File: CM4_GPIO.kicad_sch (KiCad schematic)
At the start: 17 parts, among them J1 Conn_01x02, J14 Conn_02x03_Odd_Even, J8 THD-20-R, U3 MagJack-A70-112-331N126, U5 74LVC1G07SE-7

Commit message: added a lot more parts
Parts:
- C1: value 100n -> 0.1uF; DK (none) -> 478-KGM05AR71C104KHCT-ND; PARTNO (none) -> KGM05AR71C104KH; Part Description 0.1uF 10% 16V Ceramic Capacitor X7R 0402 (1005 Metric) -> (none)
- D2: DK (none) -> 160-1478-1-ND; Field4 Digikey -> (none); Field5 LTST-S270KGKT -> (none); Field6 SML-A12M8TT86N -> (none); Field7 Rohm -> (none); Field8 650263301 -> (none); PARTNO (none) -> LTST-S270KGKT; Part Description Green 572nm LED Indication - Discrete 2.2V 2-SMD, No Lead -> (none)
- U5: DK (none) -> 1727-3099-1-ND; Field4 Farnell -> (none); Field5 2425492 -> (none); Field6 74LVC1G07SE-7 -> (none); Field7 Diodes -> (none); PARTNO (none) -> 74LVC1G07GW,125; Part Description Buffer, Non-Inverting 1 Element 1 Bit per Element Open Drai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 -> (none)
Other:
- moved on the sheet: J1
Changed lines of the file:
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@@
     (stroke (width 0) (type solid))
   )
-  (wire (pts (xy 78.105 167.64) (xy 88.265 167.64))
+  (wire (pts (xy 71.12 171.45) (xy 81.28 171.45))
     (stroke (width 0) (type default))
   )
@@
     (stroke (width 0) (type solid))
   )
-  (wire (pts (xy 78.105 165.1) (xy 88.265 165.1))
+  (wire (pts (xy 71.12 168.91) (xy 81.28 168.91))
     (stroke (width 0) (type default))
   )
@@
     (effects (font (size 1.27 1.27)) (justify left bottom))
   )
-  (text "Force RPIBOOT = Jumper Pins" (at 93.345 161.29 0)
+  (text "Force RPIBOOT = Jumper Pins" (at 86.36 165.1 0)
     (effects (font (size 1.27 1.27)) (justify right bottom))
   )
@@
     (effects (font (size 1.27 1.27)) (justify right bottom))
   )
-  (label "nRPIBOOT" (at 88.265 165.1 180) (fields_autoplaced)
+  (label "nRPIBOOT" (at 81.28 168.91 180) (fields_autoplaced)
     (effects (font (size 1.27 1.27)) (justify right bottom))
   )
@@
     (effects (font (size 1.27 1.27)) (justify right bottom))
   )
-  (label "GND" (at 79.375 167.64 0) (fields_autoplaced)
+  (label "GND" (at 72.39 171.45 0) (fields_autoplaced)
     (effects (font (size 1.27 1.27)) (justify left bottom))
   )
@@
       (effects (font (size 1.27 1.27)) hide)
     )
-    (property "Field4" "Farnell" (at 183.515 145.415 0)
-      (effects (font (size 1.27 1.27)) hide)
-    )
-    (property "Field5" "2425492" (at 183.515 145.415 0)
-      (effects (font (size 1.27 1.27)) hide)
-    )
-    (property "Field6" "74LVC1G07SE-7" (at 183.515 145.415 0)
-      (effects (font (size 1.27 1.27)) hide)
-    )
-    (property "Field7" "Diodes" (at 183.515 145.415 0)
-      (effects (font (size 1.27 1.27)) hide)
-    )
-    (property "Part Description" "Buffer, Non-Inverting 1 Element 1 Bit per Element Open Drain Output SOT-353" (at 183.515 145.415 0)
+    (property "DK" "1727-3099-1-ND" (at 183.515 145.415 0)
+      (effects (font (size 1.27 1.27)) hide)
+    )
+    (property "PARTNO" "74LVC1G07GW,125" (at 183.515 145.415 0)
       (effects (font (size 1.27 1.27)) hide)
     )
@@
       (effects (font (size 1.27 1.27)) (justify left))
     )
-    (property "Value" "100n" (at 231.521 43.053 0)
+    (property "Value" "0.1uF" (at 231.521 43.053 0)
       (effects (font (size 1.27 1.27)) (justify left))
     )
@@
       (effects (font (size 1.27 1.27)) hide)
     )
-    (property "Part Description" "	0.1uF 10% 16V Ceramic Capacitor X7R 0402 (1005 Metric)" (at 228.6 41.91 0)
+    (property "Part Description" "" (at 228.6 41.91 0)
       (effects (font (size 1.27 1.27)) hide)
     )
     (property "Field8" "110091611" (at 228.6 41.91 0)
+      (effects (font (size 1.27 1.27)) hide)
+    )
+    (property "DK" "478-KGM05AR71C104KHCT-ND" (at 228.6 41.91 0)
+      (effects (font (size 1.27 1.27)) hide)
+    )
+    (property "PARTNO" "KGM05AR71C104KH" (at 228.6 41.91 0)
       (effects (font (size 1.27 1.27)) hide)
     )
@@
       (effects (font (size 1.27 1.27)) hide)
     )
-    (property "Field4" "Digikey " (at 116.84 25.4 0)
-      (effects (font (size 1.27 1.27)) hide)
-    )
-    (property "Field5" "LTST-S270KGKT" (at 116.84 25.4 0)
-      (effects (font (size 1.27 1.27)) hide)
-    )
-    (property "Field6" "SML-A12M8TT86N" (at 116.84 25.4 0)
-      (effects (font (size 1.27 1.27)) hide)
-    )
-    (property "Field7" "Rohm" (at 116.84 25.4 0)
-      (effects (font (size 1.27 1.27)) hide)
-    )
-    (property "Field8" "650263301" (at 116.84 25.4 0)
-      (effects (font (size 1.27 1.27)) hide)
-    )
-    (property "Part Description" "	Green 572nm LED Indication - Discrete 2.2V 2-SMD, No Lead" (at 116.84 25.4 0)
+    (property "DK" "160-1478-1-ND" (at 116.84 25.4 0)
+      (effects (font (size 1.27 1.27)) hide)
+    )
+    (property "PARTNO" "LTST-S270KGKT" (at 116.84 25.4 0)
       (effects (font (size 1.27 1.27)) hide)
     )
@@
     )
   )
-  (symbol (lib_id "Connector_Generic:Conn_01x02") (at 73.025 167.64 180) (unit 1)
-    (in_bom yes) (on_board yes) (dnp no)
-    (property "Reference" "J1" (at 73.025 162.56 0)
+  (symbol (lib_id "Connector_Generic:Conn_01x02") (at 66.04 171.45 180) (unit 1)
+    (in_bom yes) (on_board yes) (dnp no)
+    (property "Reference" "J1" (at 66.04 166.37 0)
       (effects (font (size 1.27 1.27)))
     )
-    (property "Value" "Conn_01x02" (at 73.025 161.29 0)
-      (effects (font (size 1.27 1.27)) hide)
-    )
-    (property "Footprint" "Connector_PinHeader_2.54mm:PinHeader_1x02_P2.54mm_Vertical" (at 73.025 167.64 0)
-      (effects (font (size 1.27 1.27)) hide)
-    )
-    (property "Datasheet" "~" (at 73.025 167.64 0)
-      (effects (font (size 1.27 1.27)) hide)
-    )
+    (property "Value" "Conn_01x02" (at 66.04 165.1 0)
+      (effects (font (size 1.27 1.27)) hide)
+    )
+    (property "Footprint" "Connector_PinHeader_2.54mm:PinHeader_1x02_P2.54mm_Vertical" (at 66.04 171.45 0)
+      (effects (font (size 1.27 1.27)) hide)
+    )
+    (property "Datasheet" "~" (at 66.04 171.45 0)
+      (effects (font (size 1.27 1.27)) hide)
+    )

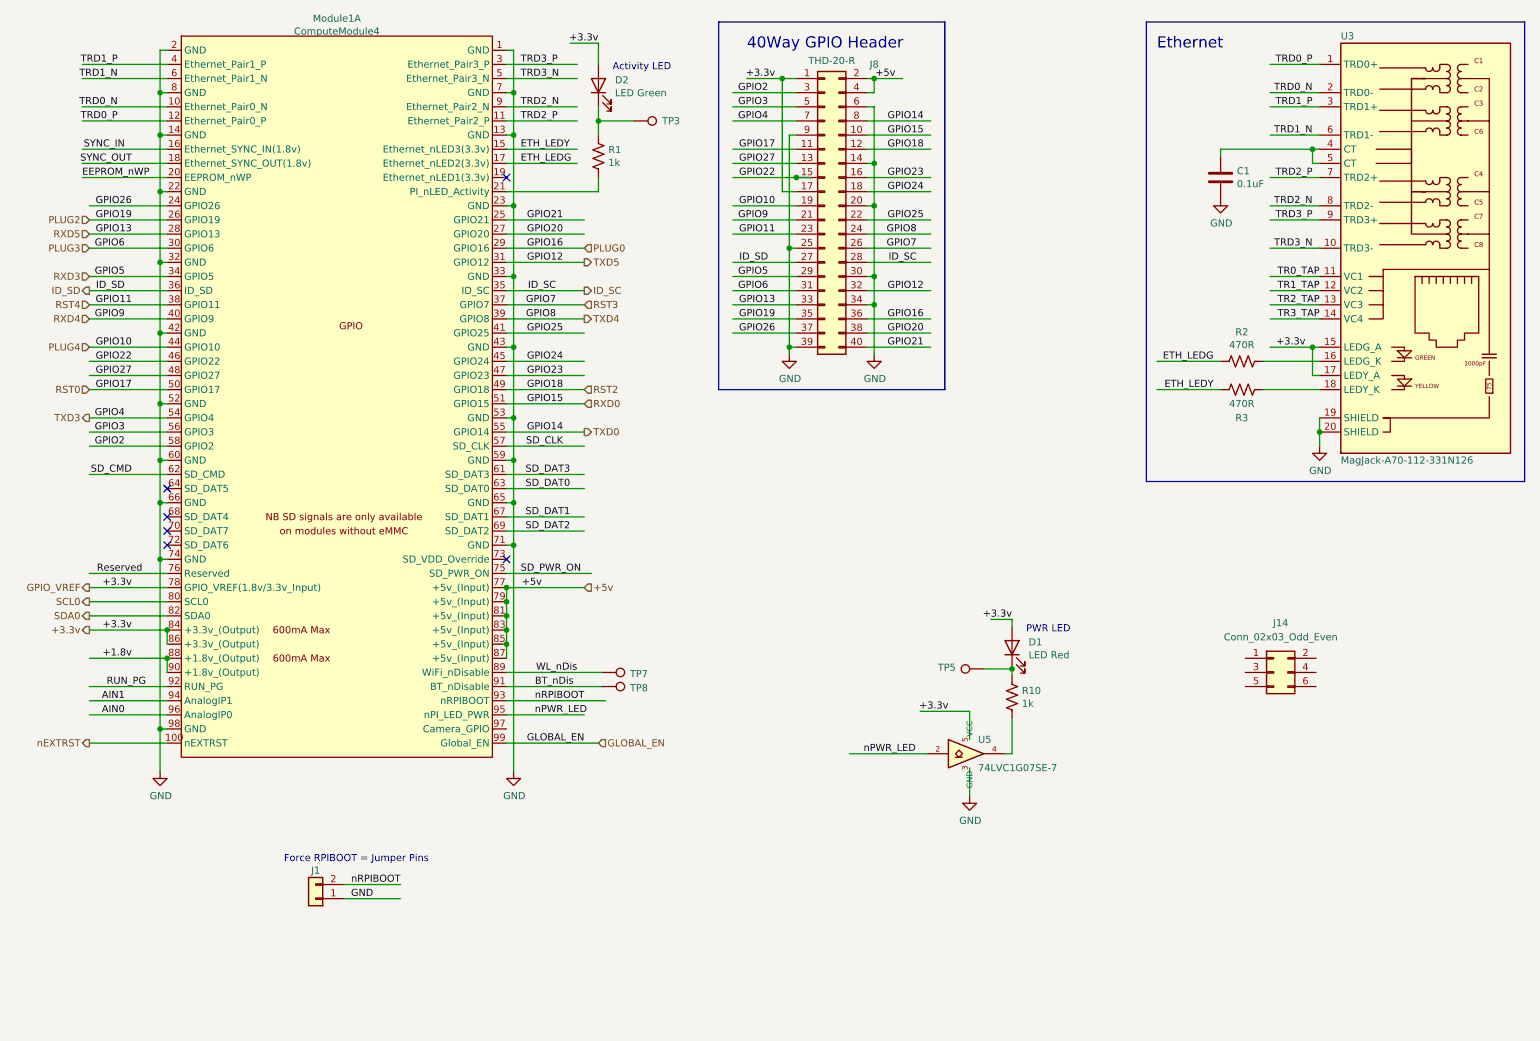
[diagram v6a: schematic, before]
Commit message: resolved some schematic-board errors. switched to tap-on-top ethernet.
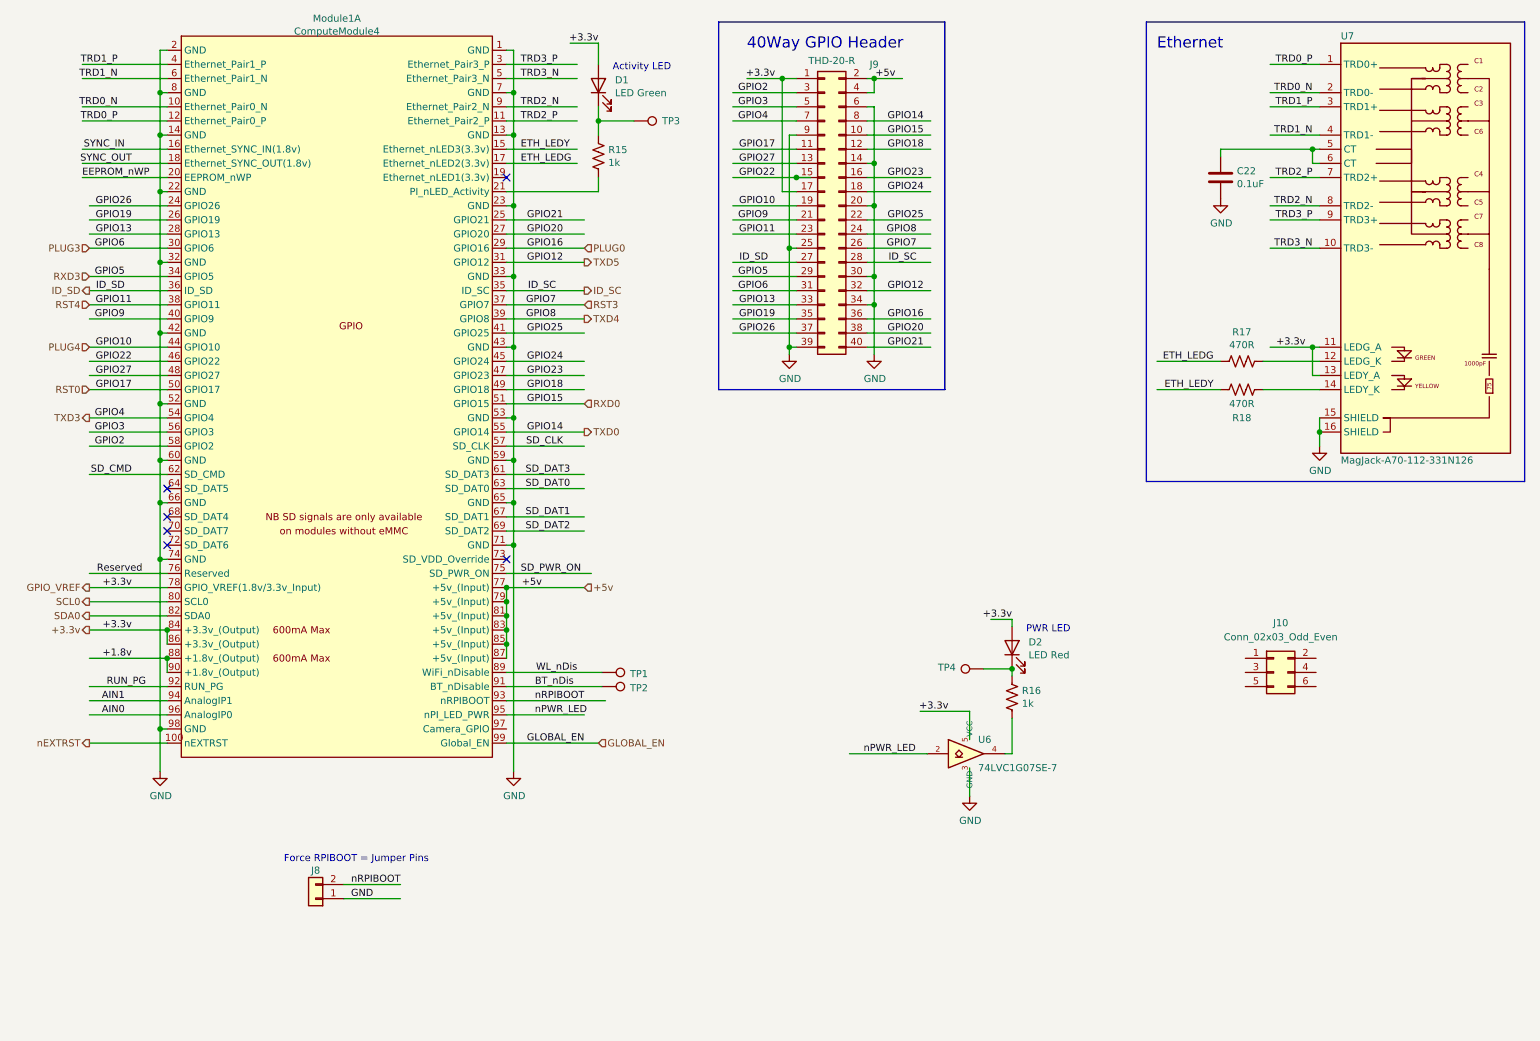
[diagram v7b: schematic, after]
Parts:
- U6: renamed from U5; symbol CM4IO:74LVC1G07_copy -> bitcart:74LVC1G07
- U7: renamed from U3; footprint CM4IO:TRJG0926HENL -> bitcart:ARJM11D7-502-AB-EW2_ABR; symbol CM4IO:MagJack-A70-112-331N126 -> bitcart:ARJM11D7-502-AB-EW2; DK (none) -> 535-14152-ND; PARTNO (none) -> ARJM11D7-502-AB-EW2
- renumbered C1 to C22, D2 to D1, D1 to D2, J14 to J10, J1 to J8, J8 to J9, R1 to R15, R10 to R16, R2 to R17, R3 to R18, TP7 to TP1, TP8 to TP2, TP5 to TP4
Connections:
- net TR0_TAP is gone; now on net +3.3v: U7.11 (LEDG_A)
- net TR1_TAP is gone; now on an unnamed net: U7.12 (LEDG_K)
- net TR2_TAP is gone; now on net +3.3v: U7.13 (LEDY_A)
- net TR3_TAP is gone; now on an unnamed net: U7.14 (LEDY_K)
- net +3.3v: no longer U7.15 (LEDG_A), U7.17 (LEDY_A)
- net GND: now also U7.15 (SHIELD), U7.16 (SHIELD); no longer U7.19 (SHIELD), U7.20 (SHIELD)
- net TRD1_N: now also U7.4 (TRD1-); no longer U7.6 (TRD1-)
- net at R17.1: no longer U7.16 (LEDG_K)
- net at R18.1: no longer U7.18 (LEDY_K)
- net at C22.1, U7.5 (CT): now also U7.6 (CT); no longer U7.4 (CT)
- net PLUG2 renamed GPIO19
- net RST2 renamed GPIO18
- net RXD4 renamed GPIO9
- net RXD5 renamed GPIO13
